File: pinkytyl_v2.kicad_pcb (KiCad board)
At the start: 2 copper layers, 132.2 x 106 mm, 57 parts, among them J1 AudioJack3, J3 USB_B_Mini, J5 Conn_02x05_Odd_Even, K0 KEYSW, K10 KEYSW, K11 KEYSW, K12 KEYSW, K13 KEYSW, K14 KEYSW, K15 KEYSW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

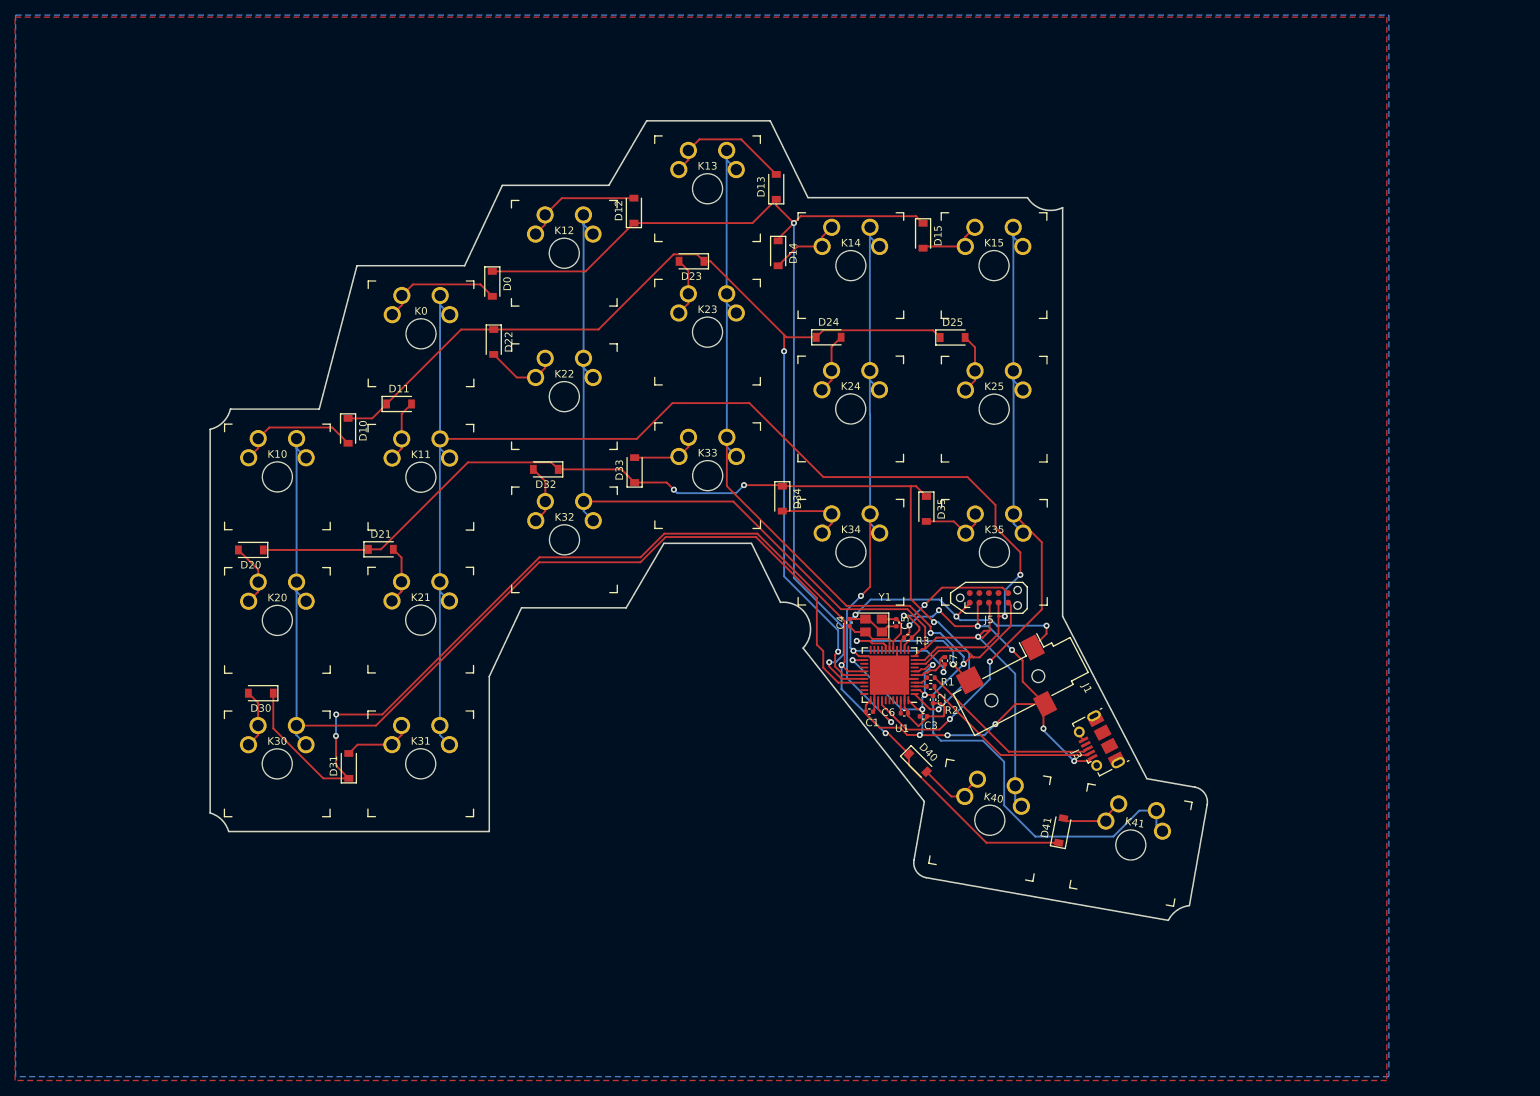
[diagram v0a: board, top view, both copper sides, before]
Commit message: Adds smaller version of the 3.5mm connector
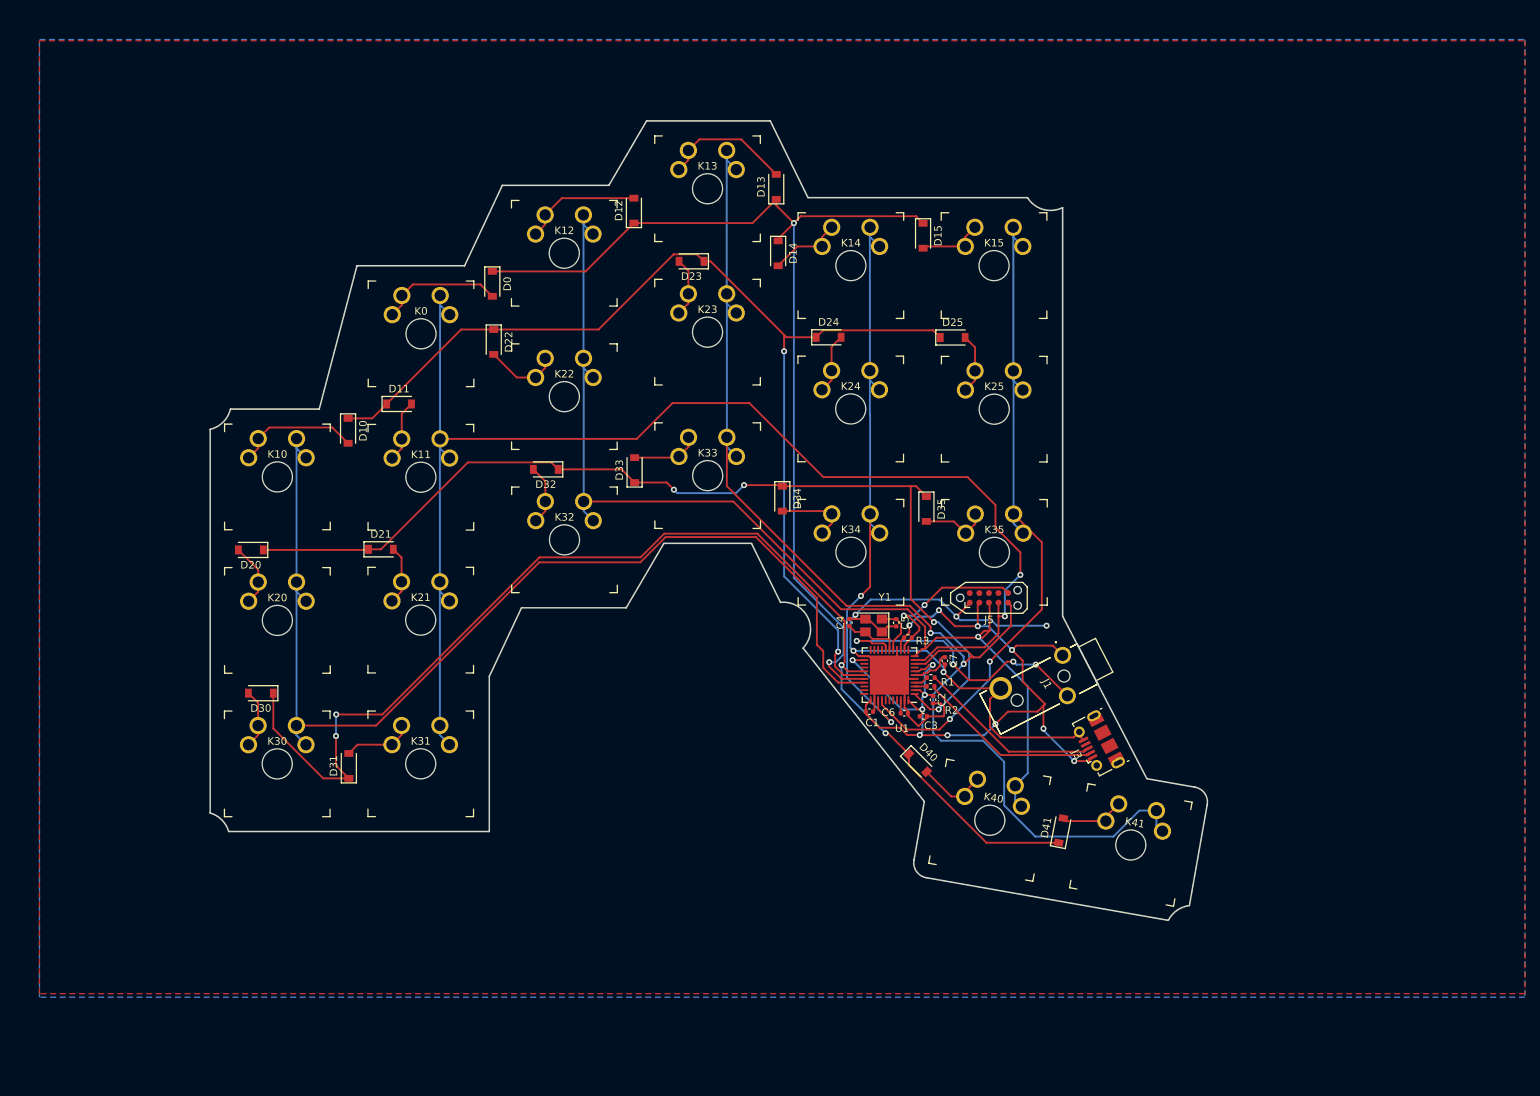
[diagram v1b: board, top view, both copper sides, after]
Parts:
- J1: value AudioJack3 -> STX-3501-3N; footprint Connector_Audio:Jack_3.5mm_CUI_SJ-3523-SMT_Horizontal -> STX-3501-3N:STX35013N
- moved J1 6.70 mm to (183.7, 107.0), turned to 297.3 degrees
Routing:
- net GND: track 97.2 -> 120.5 mm
- net serial: track 22.9 -> 38.8 mm, vias 2 -> 4
- net VCC: track 105.7 -> 113.2 mm
- net MISO: track 143.3 -> 144.7 mm

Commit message: Cound be final
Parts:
- added J2: Conn_01x02, Connector_PinHeader_1.27mm:PinHeader_1x02_P1.27mm_Vertical, F.Cu at (179.1, 104.5)
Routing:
- net reset: track 22.2 -> 33.0 mm, vias 2 -> 4
- net GND: track 120.5 -> 122.4 mm
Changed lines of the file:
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@@
     (thickness 1.6)
     (drawings 152)
-    (tracks 585)
+    (tracks 595)
     (zones 0)
-    (modules 57)
+    (modules 58)
     (nets 64)
   )
@@
     (add_net serial)
   )
+  (module Connector_PinHeader_1.27mm:PinHeader_1x02_P1.27mm_Vertical (layer F.Cu)
+    (at 179.05 104.48 90)
+    (descr "Through hole straight pin header, 1x02, 1.27mm pitch, single row")
+    (tags "Through hole pin header THT 1x02 1.27mm single row")
+    (fp_text reference J2 (at -2.51 0.31 90) (layer F.SilkS)
+      (effects (font (size 1 1) (thickness 0.15)))
+    )
+    (fp_text value Conn_01x02 (at 0 2.965 90) (layer F.Fab)
+      (effects (font (size 1 1) (thickness 0.15)))
+    )
+    (fp_text user %R (at 0 0.635) (layer F.Fab)
+      (effects (font (size 1 1) (thickness 0.15)))
+    )
+    (fp_line (start -0.525 -0.635) (end 1.05 -0.635) (layer F.Fab) (width 0.1))
+    (fp_line (start 1.05 -0.635) (end 1.05 1.905) (layer F.Fab) (width 0.1))
+    (fp_line (start 1.05 1.905) (end -1.05 1.905) (layer F.Fab) (width 0.1))
+    (fp_line (start -1.05 1.905) (end -1.05 -0.11) (layer F.Fab) (width 0.1))
+    (fp_line (start -1.05 -0.11) (end -0.525 -0.635) (layer F.Fab) (width 0.1))
+    (fp_line (start -1.11 1.965) (end -0.30753 1.965) (layer F.SilkS) (width 0.12))
+    (fp_line (start 0.30753 1.965) (end 1.11 1.965) (layer F.SilkS) (width 0.12))
+    (fp_line (start -1.11 0.76) (end -1.11 1.965) (layer F.SilkS) (width 0.12))
+    (fp_line (start 1.11 0.76) (end 1.11 1.965) (layer F.SilkS) (width 0.12))
+    (fp_line (start -1.11 0.76) (end -0.563471 0.76) (layer F.SilkS) (width 0.12))
+    (fp_line (start 0.563471 0.76) (end 1.11 0.76) (layer F.SilkS) (width 0.12))
+    (fp_line (start -1.11 0) (end -1.11 -0.76) (layer F.SilkS) (width 0.12))
+    (fp_line (start -1.11 -0.76) (end 0 -0.76) (layer F.SilkS) (width 0.12))
+    (fp_line (start -1.55 -1.15) (end -1.55 2.45) (layer F.CrtYd) (width 0.05))
+    (fp_line (start -1.55 2.45) (end 1.55 2.45) (layer F.CrtYd) (width 0.05))
+    (fp_line (start 1.55 2.45) (end 1.55 -1.15) (layer F.CrtYd) (width 0.05))
+    (fp_line (start 1.55 -1.15) (end -1.55 -1.15) (layer F.CrtYd) (width 0.05))
+    (pad 2 thru_hole oval (at 0 1.27 90) (size 1 1) (drill 0.65) (layers *.Cu *.Mask)
+      (net 2 GND))
+    (pad 1 thru_hole rect (at 0 0 90) (size 1 1) (drill 0.65) (layers *.Cu *.Mask)
+      (net 38 reset))
+    (model ${KISYS3DMOD}/Connector_PinHeader_1.27mm.3dshapes/PinHeader_1x02_P1.27mm_Vertical.wrl
+      (at (xyz 0 0 0))
+      (scale (xyz 1 1 1))
+      (rotate (xyz 0 0 0))
+    )
+  )
   (module STX-3501-3N:STX35013N (layer F.Cu)
     (at 183.67 106.99 297.3)
@@
   (segment (start 185.157442 117.871323) (end 175.448321 117.871323) (width 0.25) (layer F.Cu) (net 2))
   (segment (start 185.882441 117.146324) (end 185.157442 117.871323) (width 0.25) (layer F.Cu) (net 2))
+  (segment (start 180.32 104.28) (end 181.54 103.06) (width 0.25) (layer F.Cu) (net 2))
+  (segment (start 180.32 104.48) (end 180.32 104.28) (width 0.25) (layer F.Cu) (net 2))
   (segment (start 156.16 103.89) (end 155.4 103.13) (width 0.25) (layer F.Cu) (net 3))
   (segment (start 157.53 103.89) (end 156.16 103.89) (width 0.25) (layer F.Cu) (net 3))
@@
   (segment (start 164.68 103.65) (end 164.68 103.23) (width 0.25) (layer F.Cu) (net 38))
   (segment (start 163.68 104.65) (end 164.68 103.65) (width 0.25) (layer F.Cu) (net 38))
+  (via (at 181.72 101.33) (size 0.8) (drill 0.4) (layers F.Cu B.Cu) (net 38))
+  (segment (start 179.05 104) (end 181.72 101.33) (width 0.25) (layer F.Cu) (net 38))
+  (segment (start 179.05 104.48) (end 179.05 104) (width 0.25) (layer F.Cu) (net 38))
+  (via (at 180.1 99.38) (size 0.8) (drill 0.4) (layers F.Cu B.Cu) (net 38))
+  (segment (start 180.1 99.71) (end 180.1 99.38) (width 0.25) (layer B.Cu) (net 38))
+  (segment (start 181.72 101.33) (end 180.1 99.71) (width 0.25) (layer B.Cu) (net 38))
+  (segment (start 177.085 99.38) (end 176.44 98.735) (width 0.25) (layer F.Cu) (net 38))
+  (segment (start 180.1 99.38) (end 177.085 99.38) (width 0.25) (layer F.Cu) (net 38))
   (segment (start 82.12 78.26) (end 82.12 97.28) (width 0.25) (layer B.Cu) (net 43))
   (segment (start 82.12 116.28) (end 82.1 116.3) (width 0.25) (layer B.Cu) (net 43))
@@
     (polygon
       (pts
-        (xy 244.95 151.84) (xy 48.04 151.84) (xy 48.04 25.52) (xy 244.95 25.52)
+        (xy 218.98 149.33) (xy 53.45 149.33) (xy 53.45 28.53) (xy 218.98 28.53)
       )
     )
@@
     (polygon
       (pts
-        (xy 244.95 152.31) (xy 48.04 152.31) (xy 48.04 25.36) (xy 244.95 25.36)
+        (xy 218.98 149.01) (xy 53.45 149.01) (xy 53.45 28.8) (xy 218.98 28.8)
       )
     )

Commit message: In the middle of slim redesign
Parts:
- J1: value STX-3501-3N -> 50-00174; footprint STX-3501-3N:STX35013N -> misc:54-00174
- moved J3 103.5 mm to (117.8, 42.9), turned to 180 degrees
- moved J1 60.7 mm to (187.5, 46.4), turned to 270 degrees
- moved J5 22.0 mm to (195.9, 99.5)
- moved J2 21.4 mm to (200.1, 108.2)
- moved R1 11.1 mm to (177.2, 111.4)
- moved R2 11.1 mm to (177.1, 112.6)
- moved R3 11.1 mm to (174.1, 106.1)
- moved Y1 11.1 mm to (169.6, 104.5)
- moved C1 11.1 mm to (169.0, 116.0)
- moved C7 11.1 mm to (179.0, 109.2)
- moved C2 11.1 mm to (177.4, 114.4)
- moved C3 11.1 mm to (176.2, 116.6)
- moved C4 11.1 mm to (166.3, 104.1)
- moved C5 11.1 mm to (172.6, 104.2)
- moved C6 11.1 mm to (173.6, 116.2)
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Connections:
- J1 pad 2: GND -> serial
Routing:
- net MOSI: track 185.0 -> 0.00 mm, vias 2 -> 0
- net c3: track 171.3 -> 0.00 mm, vias 2 -> 0
- net r0: track 159.4 -> 0.00 mm, vias 4 -> 0
- net c0: track 145.8 -> 0.00 mm
- net MISO: track 144.7 -> 0.00 mm, vias 1 -> 0
- net r2: track 144.3 -> 0.00 mm, vias 2 -> 0
- net r3: track 135.0 -> 0.00 mm, vias 2 -> 0
- net r1: track 134.3 -> 0.00 mm, vias 4 -> 0
- net GND: track 122.4 -> 0.00 mm, vias 5 -> 0
- net VCC: track 113.2 -> 0.00 mm, vias 13 -> 0
- net c5: track 92.6 -> 0.00 mm, vias 2 -> 0
- net c4: track 82.1 -> 0.00 mm, vias 2 -> 0
- net serial: track 38.8 -> 0.00 mm, vias 4 -> 0
- net reset: track 33.0 -> 0.00 mm, vias 4 -> 0
- net d-: track 24.7 -> 0.00 mm
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- removed copper zone on B.Cu, net GND
- removed copper zone on F.Cu, net GND
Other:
- board size 132.2 x 106 mm -> 132 x 105.9 mm

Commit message: Inc
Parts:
- moved J3 0.12 mm to (117.8, 43.0)
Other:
- outline, holes or cut-outs redrawn

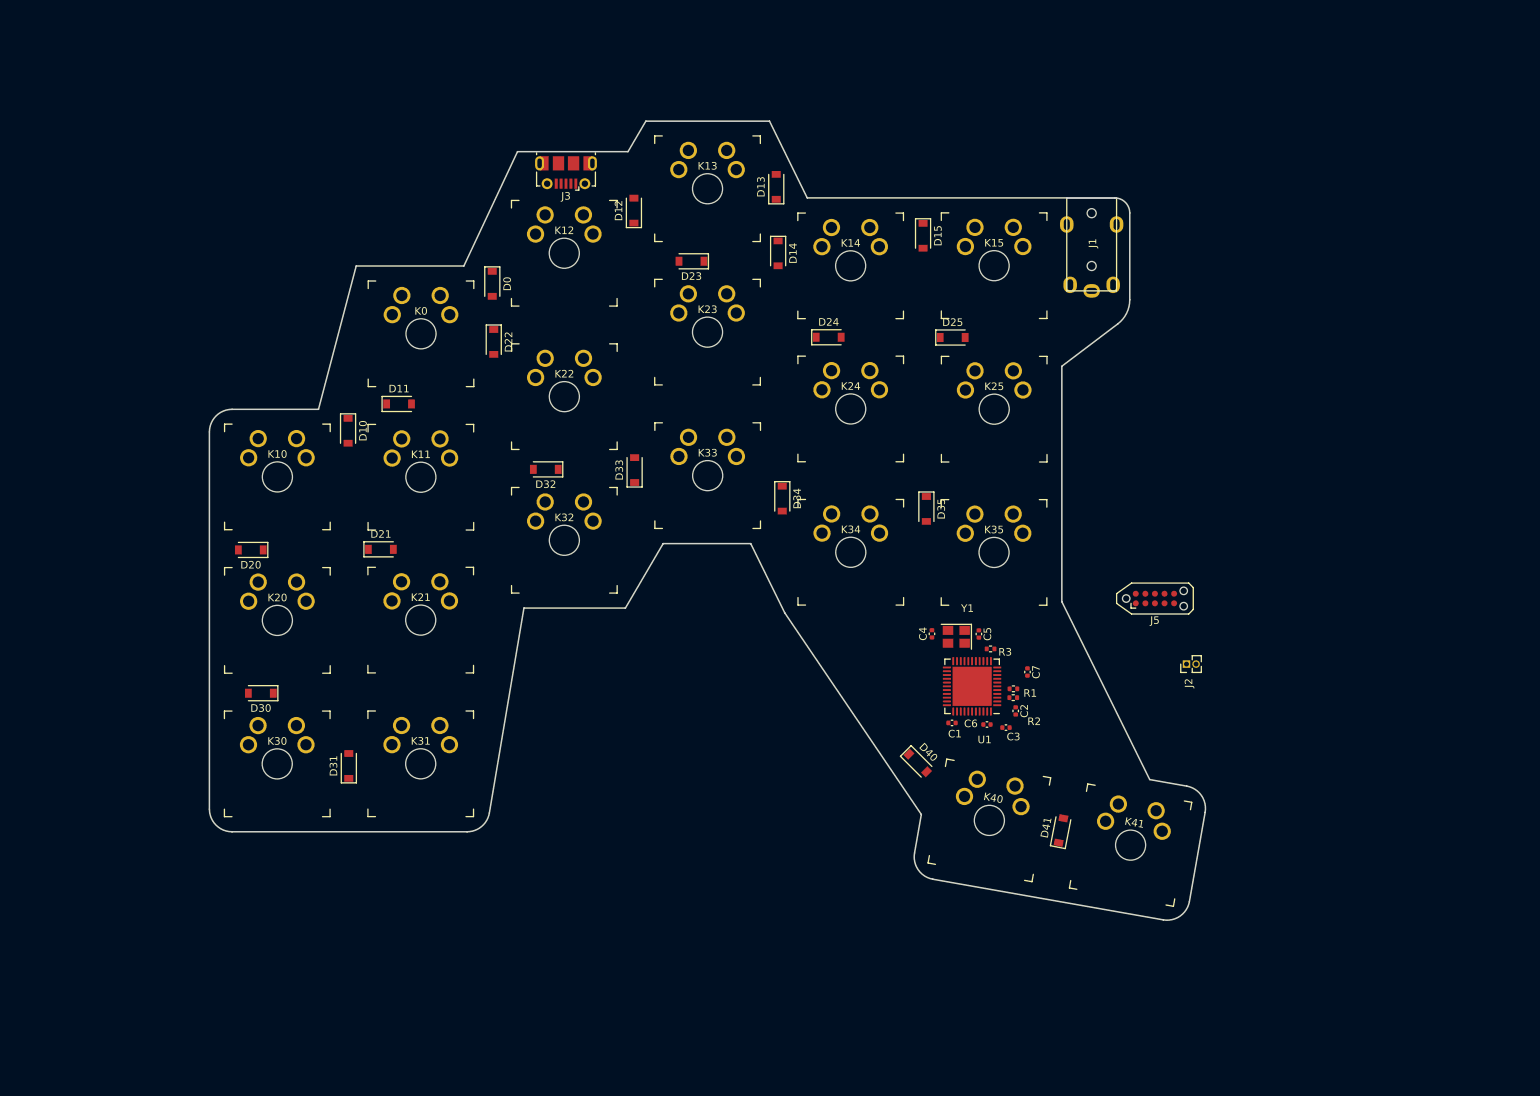
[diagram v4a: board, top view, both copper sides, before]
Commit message: Keys wired
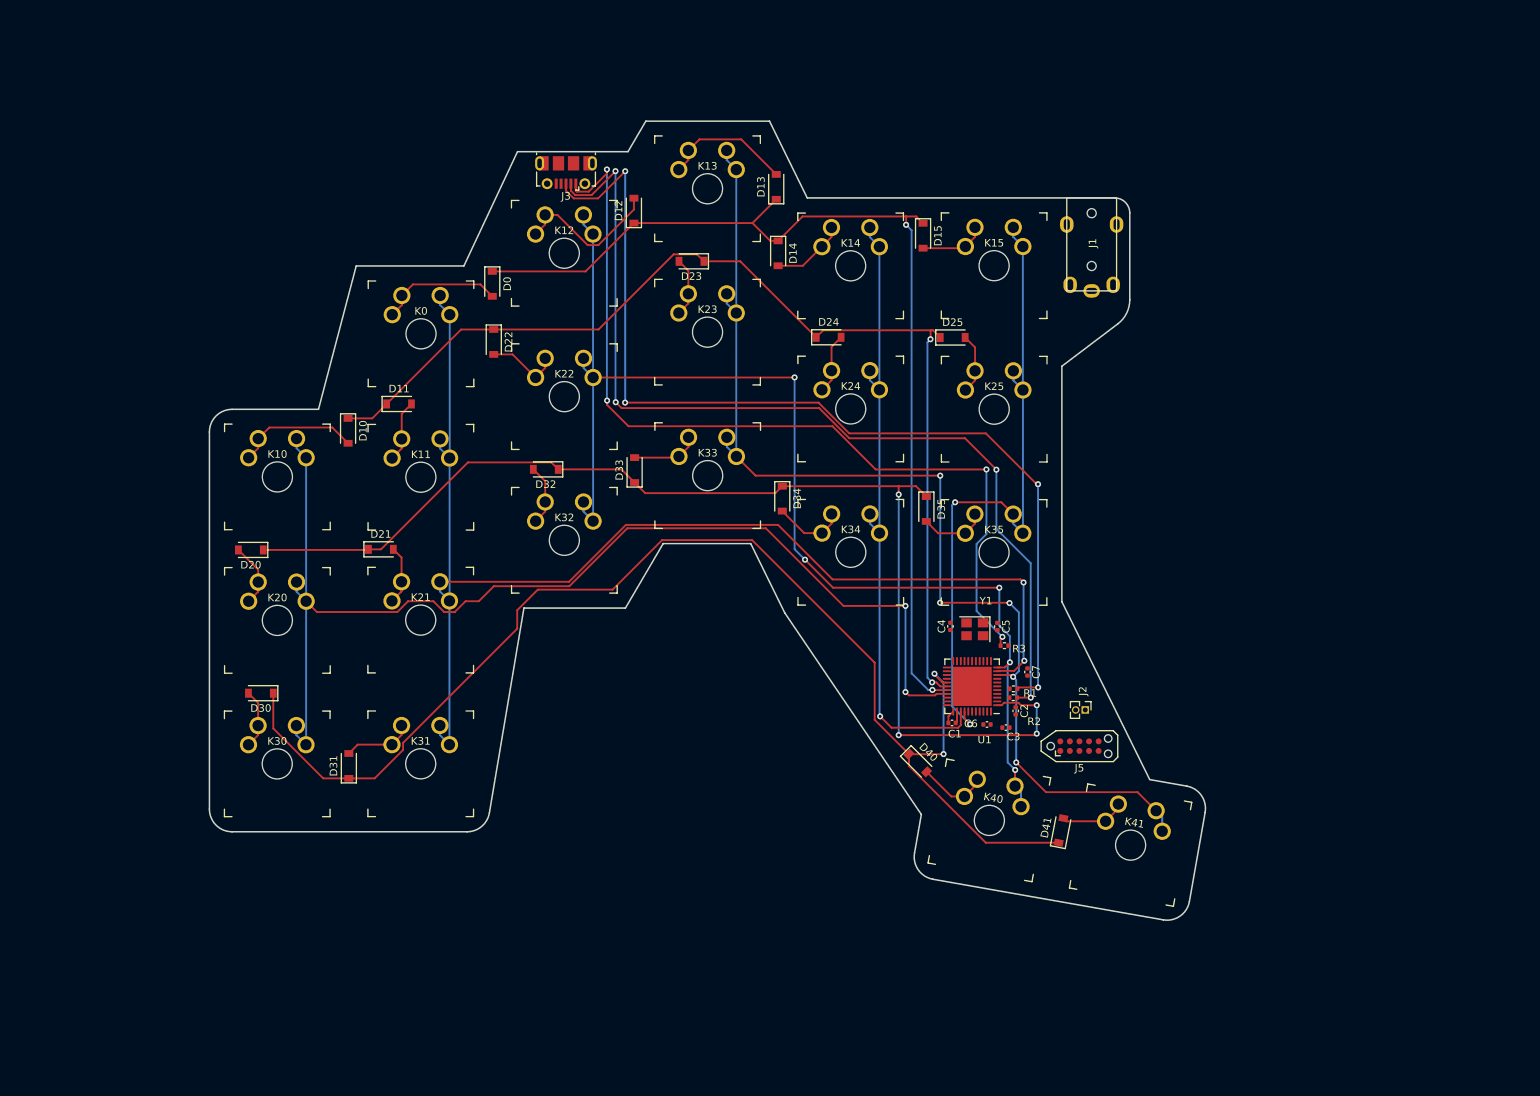
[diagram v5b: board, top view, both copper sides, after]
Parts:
- moved J5 22.0 mm to (185.9, 119.0)
- moved J2 14.7 mm to (186.7, 114.2), turned to 270 degrees
- moved C4 2.64 mm to (168.8, 103.2)
- moved C5 2.64 mm to (175.0, 103.2)
- moved Y1 2.64 mm to (172.0, 103.5)
- moved R3 1.89 mm to (176.0, 105.7)
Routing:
- net MOSI: track 0.00 -> 167.5 mm, vias 0 -> 2
- net r0: track 0.00 -> 166.5 mm, vias 0 -> 2
- net MISO: track 0.00 -> 158.4 mm, vias 0 -> 5
- net r1: track 0.00 -> 156.0 mm, vias 0 -> 4
- net c0: track 0.00 -> 154.5 mm, vias 0 -> 2
- net c3: track 0.00 -> 150.0 mm, vias 0 -> 5
- net r2: track 0.00 -> 142.1 mm, vias 0 -> 2
- net r3: track 0.00 -> 133.4 mm, vias 0 -> 2
- net d+: track 0.00 -> 130.4 mm, vias 0 -> 4
- net d-: track 0.00 -> 127.1 mm, vias 0 -> 4
- net VCC: track 0.00 -> 118.9 mm, vias 0 -> 4
- net c5: track 0.00 -> 88.1 mm, vias 0 -> 2
- net c4: track 0.00 -> 84.8 mm, vias 0 -> 1
- net Net-(D12-Pad2): track 0.00 -> 20.0 mm
- net Net-(D13-Pad2): track 0.00 -> 17.2 mm
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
